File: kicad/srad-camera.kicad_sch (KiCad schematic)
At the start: 21 parts, among them J1 DEBUG, SW1 POWER, SW2 USER, SW3 BOOT0

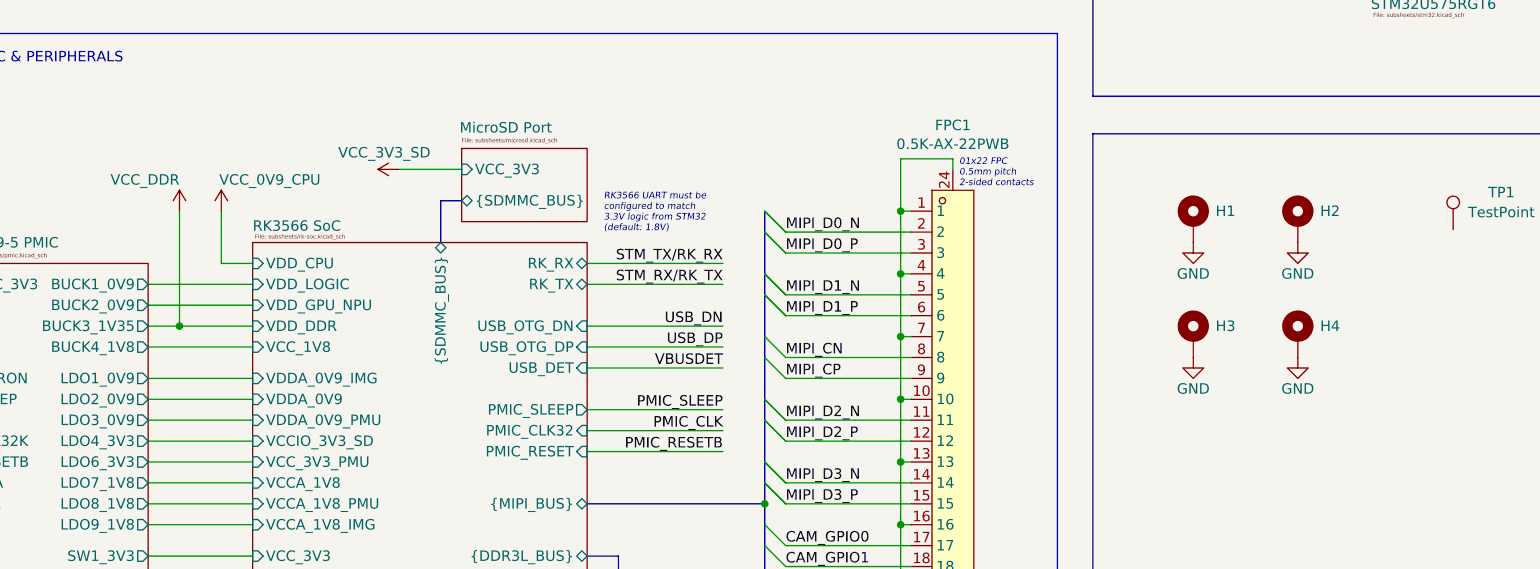
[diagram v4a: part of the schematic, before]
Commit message: All major components placed on board
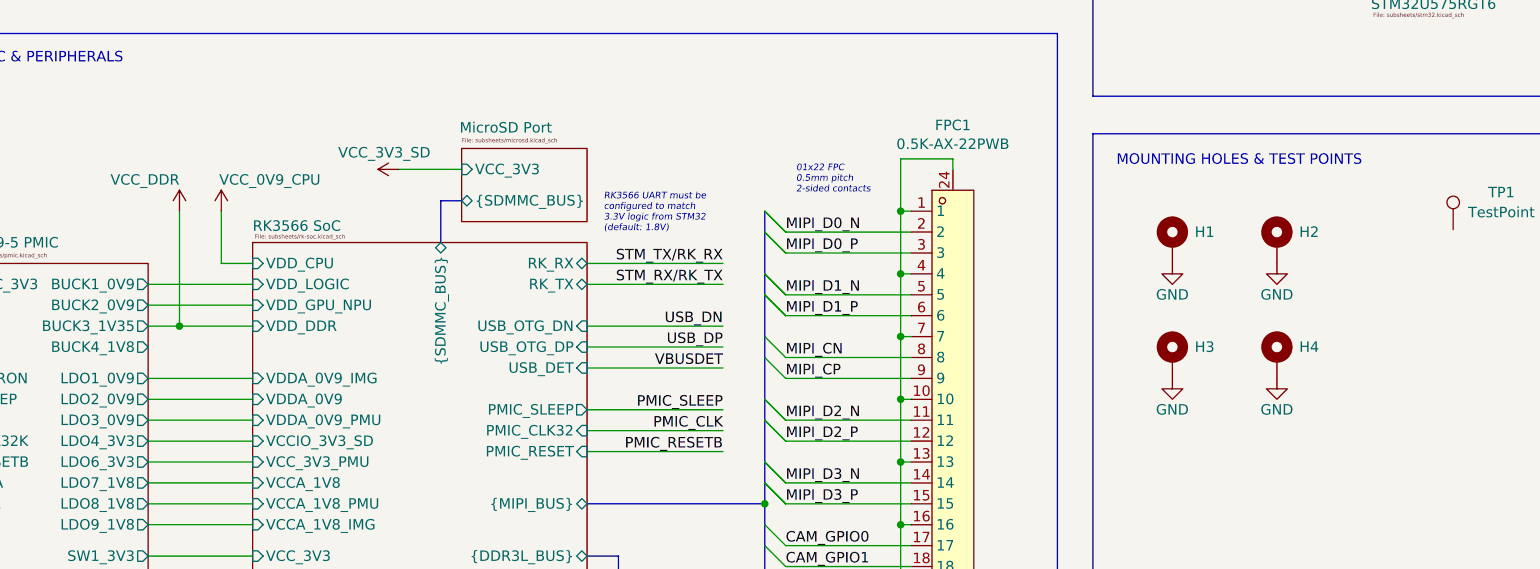
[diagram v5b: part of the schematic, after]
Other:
- sheet RK3566 SoC ports: added none; removed VCC_1V8
- note added: "MOUNTING HOLES & TEST POINTS"
- moved on the sheet: H1, H2, H3, H4
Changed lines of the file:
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@@
 	(text "01x22 FPC\n0.5mm pitch\n2-sided contacts"
 		(exclude_from_sim no)
-		(at 160.782 107.188 0)
+		(at 140.97 107.95 0)
 		(effects
 			(font
@@
 		)
 	)
+	(text "MOUNTING HOLES & TEST POINTS"
+		(exclude_from_sim no)
+		(at 194.818 105.664 0)
+		(effects
+			(font
+				(size 1.27 1.27)
+			)
+		)
+	)
 	(junction
 		(at 153.67 127)
@@
 		)
 	)
-	(wire
-		(pts
-			(xy 62.23 128.27) (xy 74.93 128.27)
-		)
-		(stroke
-			(width 0)
-			(type default)
-		)
-	)
 	(bus
 		(pts
@@
 		)
 	)
-	(rule_area
-		(polyline
-			(pts
-				(xy 150.4806 113.0631) (xy 153.0206 113.0631) (xy 153.0206 148.6231) (xy 150.4806 148.6231)
-			)
-			(stroke
-				(width 0)
-				(type dash)
-			)
-			(fill
-				(type none)
-			)
-		)
-	)
-	(netclass_flag ""
-		(length 2.54)
-		(shape round)
-		(at 151.7506 113.0631 0)
-		(fields_autoplaced yes)
-		(effects
-			(font
-				(size 1.27 1.27)
-			)
-			(justify left bottom)
-		)
-		(property "Netclass" "MIPI_DIFF"
-			(at 151.0521 110.5231 0)
-			(effects
-				(font
-					(size 1 1)
-					(italic yes)
-					(color 0 132 132 1)
-				)
-				(justify right)
-			)
-		)
-		(property "Component Class" ""
-			(at 320.6606 -2.5069 0)
-			(effects
-				(font
-					(size 1.27 1.27)
-					(italic yes)
-				)
-				(justify left)
-			)
-		)
-	)
 	(symbol
 		(lib_id "power:GND")
-		(at 189.23 115.57 0)
+		(at 186.69 118.11 0)
 		(unit 1)
 		(exclude_from_sim no)
@@
 		(dnp no)
 		(property "Reference" "#PWR013"
-			(at 189.23 121.92 0)
+			(at 186.69 124.46 0)
 			(effects
 				(font
@@
 		)
 		(property "Value" "GND"
-			(at 189.23 119.38 0)
+			(at 186.69 121.92 0)
 			(effects
 				(font
@@
 		)
 		(property "Footprint" ""
-			(at 189.23 115.57 0)
+			(at 186.69 118.11 0)
 			(effects
 				(font
@@
 		)
 		(property "Datasheet" ""
-			(at 189.23 115.57 0)
+			(at 186.69 118.11 0)
 			(effects
 				(font
@@
 		)
 		(property "Description" "Power symbol creates a global label with name \"GND\" , ground"
-			(at 189.23 115.57 0)
+			(at 186.69 118.11 0)
 			(effects
 				(font
@@
 		(lib_name "MountingHole_Pad_MP_1")
 		(lib_id "Mechanical:MountingHole_Pad_MP")
-		(at 189.23 113.03 0)
+		(at 186.69 115.57 0)
 		(unit 1)
 		(exclude_from_sim no)
@@
 		(fields_autoplaced yes)
 		(property "Reference" "H1"
-			(at 193.1512 111.76 0)
+			(at 190.6112 114.3 0)
 			(effects
 				(font
@@
 		)
 		(property "Value" "MntHole"
-			(at 202.3736 112.9721 0)
+			(at 199.8336 115.5121 0)
 			(effects
 				(font
@@
 		)
 		(property "Footprint" "srad-camera-footprints:4-40_MountingHole"
-			(at 189.23 113.03 0)
+			(at 186.69 115.57 0)
 			(effects
 				(font
@@
 		)
 		(property "Datasheet" "~"
-			(at 189.23 113.03 0)
+			(at 186.69 115.57 0)
 			(effects
 				(font
@@
 		)
 		(property "Description" "Mounting Hole with connection as pad named MP"
-			(at 189.23 113.03 0)
+			(at 186.69 115.57 0)
 			(effects
 				(font
@@
 	(symbol
 		(lib_id "power:GND")
-		(at 201.93 129.54 0)
+		(at 199.39 132.08 0)
 		(unit 1)
 		(exclude_from_sim no)
@@
 		(dnp no)
 		(property "Reference" "#PWR016"
-			(at 201.93 135.89 0)
+			(at 199.39 138.43 0)
 			(effects
 				(font
@@
 		)
 		(property "Value" "GND"
-			(at 201.93 133.35 0)
+			(at 199.39 135.89 0)
 			(effects
 				(font
@@
 		)
 		(property "Footprint" ""
-			(at 201.93 129.54 0)
+			(at 199.39 132.08 0)
 			(effects
 				(font
@@
 		)
 		(property "Datasheet" ""
-			(at 201.93 129.54 0)
+			(at 199.39 132.08 0)
 			(effects
 				(font
@@
 		)
 		(property "Description" "Power symbol creates a global label with name \"GND\" , ground"
-			(at 201.93 129.54 0)
+			(at 199.39 132.08 0)
 			(effects
 				(font
@@
 		(lib_name "MountingHole_Pad_MP_1")
 		(lib_id "Mechanical:MountingHole_Pad_MP")
-		(at 201.93 113.03 0)
+		(at 199.39 115.57 0)
 		(unit 1)
 		(exclude_from_sim no)
@@
 		(fields_autoplaced yes)
 		(property "Reference" "H2"
-			(at 205.8512 111.76 0)
+			(at 203.3112 114.3 0)
 			(effects
 				(font
@@
 		)
 		(property "Value" "MntHole"
-			(at 215.0736 112.9721 0)
+			(at 212.5336 115.5121 0)
 			(effects
 				(font
@@
 		)
 		(property "Footprint" "srad-camera-footprints:4-40_MountingHole"
-			(at 201.93 113.03 0)
+			(at 199.39 115.57 0)
 			(effects
 				(font
@@
 		)
 		(property "Datasheet" "~"
-			(at 201.93 113.03 0)
+			(at 199.39 115.57 0)
 			(effects
 				(font
@@
 		)
 		(property "Description" "Mounting Hole with connection as pad named MP"
-			(at 201.93 113.03 0)
+			(at 199.39 115.57 0)
 			(effects
 				(font
@@
 	(symbol
 		(lib_id "power:GND")
-		(at 189.23 129.54 0)
+		(at 186.69 132.08 0)
 		(unit 1)
 		(exclude_from_sim no)
@@
 		(dnp no)
 		(property "Reference" "#PWR015"
-			(at 189.23 135.89 0)
+			(at 186.69 138.43 0)
 			(effects
 				(font
@@
 		)
 		(property "Value" "GND"
-			(at 189.23 133.35 0)
+			(at 186.69 135.89 0)
 			(effects
 				(font
@@
 		)
 		(property "Footprint" ""
-			(at 189.23 129.54 0)
+			(at 186.69 132.08 0)
 			(effects
 				(font
@@
 		)
 		(property "Datasheet" ""
-			(at 189.23 129.54 0)
+			(at 186.69 132.08 0)
 			(effects
 				(font
@@
 		)
 		(property "Description" "Power symbol creates a global label with name \"GND\" , ground"
-			(at 189.23 129.54 0)
+			(at 186.69 132.08 0)
 			(effects
 				(font
@@
 		(lib_name "MountingHole_Pad_MP_1")
 		(lib_id "Mechanical:MountingHole_Pad_MP")
-		(at 201.93 127 0)
+		(at 199.39 129.54 0)
 		(unit 1)
 		(exclude_from_sim no)
@@
 		(fields_autoplaced yes)
 		(property "Reference" "H4"
-			(at 205.8512 125.73 0)
+			(at 203.3112 128.27 0)
 			(effects
 				(font
@@
 		)
 		(property "Value" "MntHole"
-			(at 215.0736 126.9421 0)
+			(at 212.5336 129.4821 0)
 			(effects
 				(font
@@
 		)
 		(property "Footprint" "srad-camera-footprints:4-40_MountingHole"
-			(at 201.93 127 0)
+			(at 199.39 129.54 0)
 			(effects
 				(font
@@
 		)
 		(property "Datasheet" "~"
-			(at 201.93 127 0)
+			(at 199.39 129.54 0)
 			(effects
 				(font
@@
 		)
 		(property "Description" "Mounting Hole with connection as pad named MP"
-			(at 201.93 127 0)
+			(at 199.39 129.54 0)
 			(effects
 				(font
@@
 		(lib_name "MountingHole_Pad_MP_1")
 		(lib_id "Mechanical:MountingHole_Pad_MP")
-		(at 189.23 127 0)
+		(at 186.69 129.54 0)
 		(unit 1)
 		(exclude_from_sim no)
@@
 		(fields_autoplaced yes)
 		(property "Reference" "H3"
-			(at 193.1512 125.73 0)
+			(at 190.6112 128.27 0)
 			(effects
 				(font
@@
 		)
 		(property "Value" "MntHole"
-			(at 202.3736 126.9421 0)
+			(at 199.8336 129.4821 0)
 			(effects
 				(font
@@
 		)
 		(property "Footprint" "srad-camera-footprints:4-40_MountingHole"
-			(at 189.23 127 0)
+			(at 186.69 129.54 0)
 			(effects
 				(font
@@
 		)
 		(property "Datasheet" "~"
-			(at 189.23 127 0)
+			(at 186.69 129.54 0)
 			(effects
 				(font
@@
 		)
 		(property "Description" "Mounting Hole with connection as pad named MP"
-			(at 189.23 127 0)
+			(at 186.69 129.54 0)
 			(effects
 				(font
@@
 	(symbol
 		(lib_id "power:GND")
-		(at 201.93 115.57 0)
+		(at 199.39 118.11 0)
 		(unit 1)
 		(exclude_from_sim no)
@@
 		(dnp no)
 		(property "Reference" "#PWR014"
-			(at 201.93 121.92 0)
+			(at 199.39 124.46 0)
 			(effects
 				(font
@@
 		)
 		(property "Value" "GND"
-			(at 201.93 119.38 0)
+			(at 199.39 121.92 0)
 			(effects
 				(font
@@
 		)
 		(property "Footprint" ""
-			(at 201.93 115.57 0)
+			(at 199.39 118.11 0)
 			(effects
 				(font
@@
 		)
 		(property "Datasheet" ""
-			(at 201.93 115.57 0)
+			(at 199.39 118.11 0)
 			(effects
 				(font
@@
 		)
 		(property "Description" "Power symbol creates a global label with name \"GND\" , ground"
-			(at 201.93 115.57 0)
+			(at 199.39 118.11 0)
 			(effects
 				(font
@@
 			(effects
 				(font
-					(size 1.27 1.27)
-				)
-				(justify left)
-			)
-		)
-		(pin "VCC_1V8" input
-			(at 74.93 128.27 180)
-			(effects
-				(font

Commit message: Allllmost everything placed
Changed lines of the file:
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@@
 	)
 	(junction
+		(at 259.08 78.74)
+		(diameter 0)
+		(color 0 0 0 0)
+	)
+	(junction
 		(at 147.32 170.18)
 		(diameter 0)
@@
 	(wire
 		(pts
+			(xy 259.08 78.74) (xy 259.08 80.01)
+		)
+		(stroke
+			(width 0)
+			(type default)
+		)
+	)
+	(wire
+		(pts
 			(xy 160.02 170.18) (xy 160.02 171.45)
 		)
@@
 	(wire
 		(pts
+			(xy 259.08 77.47) (xy 259.08 78.74)
+		)
+		(stroke
+			(width 0)
+			(type default)
+		)
+	)
+	(wire
+		(pts
 			(xy 199.39 57.15) (xy 210.82 57.15)
 		)
@@
 	(wire
 		(pts
+			(xy 260.35 78.74) (xy 259.08 78.74)
+		)
+		(stroke
+			(width 0)
+			(type default)
+		)
+	)
+	(wire
+		(pts
 			(xy 115.57 156.21) (xy 118.11 156.21)
 		)
@@
 		(lib_name "VCC_9")
 		(lib_id "power:VCC")
-		(at 259.08 77.47 270)
+		(at 260.35 78.74 270)
 		(unit 1)
 		(exclude_from_sim no)
@@
 		(dnp no)
 		(property "Reference" "#PWR07"
-			(at 255.27 77.47 0)
+			(at 256.54 78.74 0)
 			(effects
 				(font
@@
 		)
 		(property "Value" "VCCIO_3V3_IMU"
-			(at 262.128 77.47 90)
+			(at 263.398 78.74 90)
 			(effects
 				(font
@@
 		)
 		(property "Footprint" ""
-			(at 259.08 77.47 0)
+			(at 260.35 78.74 0)
 			(effects
 				(font
@@
 		)
 		(property "Datasheet" ""
-			(at 259.08 77.47 0)
+			(at 260.35 78.74 0)
 			(effects
 				(font
@@
 		)
 		(property "Description" "Power symbol creates a global label with name \"VCC\""
-			(at 259.08 77.47 0)
+			(at 260.35 78.74 0)
 			(effects
 				(font
@@
 					(unit 1)
 				)
-			)
-		)
-	)
-	(symbol
-		(lib_id "power:VCC")
-		(at 259.08 80.01 270)
-		(unit 1)
-		(exclude_from_sim no)
-		(in_bom yes)
-		(on_board yes)
-		(dnp no)
-		(property "Reference" "#PWR08"
-			(at 255.27 80.01 0)
-			(effects
-				(font
-					(size 1.27 1.27)
-				)
-				(hide yes)
-			)
-		)
-		(property "Value" "VCC_3V3_SYS"
-			(at 262.128 80.01 90)
-			(effects
-				(font
-					(size 1.27 1.27)
-				)
-				(justify left)
-			)
-		)
-		(property "Footprint" ""
-			(at 259.08 80.01 0)
-			(effects
-				(font
-					(size 1.27 1.27)
-				)
-				(hide yes)
-			)
-		)
-		(property "Datasheet" ""
-			(at 259.08 80.01 0)
-			(effects
-				(font
-					(size 1.27 1.27)
-				)
-				(hide yes)
-			)
-		)
-		(property "Description" "Power symbol creates a global label with name \"VCC\""
-			(at 259.08 80.01 0)
-			(effects
-				(font
-					(size 1.27 1.27)
-				)
-				(hide yes)
-			)
-		)
-		(pin "1"
-		)
-		(instances
-			(project "srad-camera"
-				(path "/da62c771-e8c9-451f-8df1-ec995aadcb11"
-					(reference "#PWR08")
-					(unit 1)
-				)

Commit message: PCB done besides fixing screwups + length matching
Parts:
- FPC1: value 0.5K-AX-22PWB -> Amphenol_F32R 1x22; footprint srad-camera-footprints:FPC-SMD_22P-P0.50_HDGC_0.5K-AX-22PWB -> srad-camera-footprints:AMPHENOL_10051922-2210ELF
- SW1: value POWER -> PWR
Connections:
- net VCC_3V3_SYS: now also SW1.3 (C); no longer SW1.1 (A)
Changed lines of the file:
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@@
 	)
 	(no_connect
-		(at 74.93 43.18)
+		(at 199.39 36.83)
 	)
 	(no_connect
-		(at 201.93 36.83)
+		(at 74.93 43.18)
 	)
 	(bus_entry
@@
 	(wire
 		(pts
-			(xy 199.39 35.56) (xy 199.39 36.83)
-		)
-		(stroke
-			(width 0)
-			(type default)
-		)
-	)
-	(wire
-		(pts
 			(xy 115.57 140.97) (xy 132.08 140.97)
 		)
@@
 	(wire
 		(pts
+			(xy 201.93 35.56) (xy 201.93 36.83)
+		)
+		(stroke
+			(width 0)
+			(type default)
+		)
+	)
+	(wire
+		(pts
 			(xy 115.57 118.11) (xy 132.08 118.11)
 		)
@@
 			)
 		)
-		(property "Value" "POWER"
+		(property "Value" "PWR"
 			(at 197.612 40.64 90)
 			(effects
@@
 		(lib_name "VCC_11")
 		(lib_id "power:VCC")
-		(at 199.39 35.56 0)
+		(at 201.93 35.56 0)
 		(unit 1)
 		(exclude_from_sim no)
@@
 		(dnp no)
 		(property "Reference" "#PWR01"
-			(at 199.39 39.37 0)
+			(at 201.93 39.37 0)
 			(effects
 				(font
@@
 		)
 		(property "Value" "VCC_3V3_SYS"
-			(at 199.39 31.496 0)
+			(at 201.93 31.496 0)
 			(effects
 				(font
@@
 		)
 		(property "Footprint" ""
-			(at 199.39 35.56 0)
+			(at 201.93 35.56 0)
 			(effects
 				(font
@@
 		)
 		(property "Datasheet" ""
-			(at 199.39 35.56 0)
+			(at 201.93 35.56 0)
 			(effects
 				(font
@@
 		)
 		(property "Description" "Power symbol creates a global label with name \"VCC\""
-			(at 199.39 35.56 0)
+			(at 201.93 35.56 0)
 			(effects
 				(font
@@
 			)
 		)
-		(property "Value" "0.5K-AX-22PWB"
+		(property "Value" "Amphenol_F32R 1x22"
 			(at 160.02 102.87 0)
 			(effects
@@
 			)
 		)
-		(property "Footprint" "srad-camera-footprints:FPC-SMD_22P-P0.50_HDGC_0.5K-AX-22PWB"
+		(property "Footprint" "srad-camera-footprints:AMPHENOL_10051922-2210ELF"
 			(at 160.02 138.43 0)
 			(effects

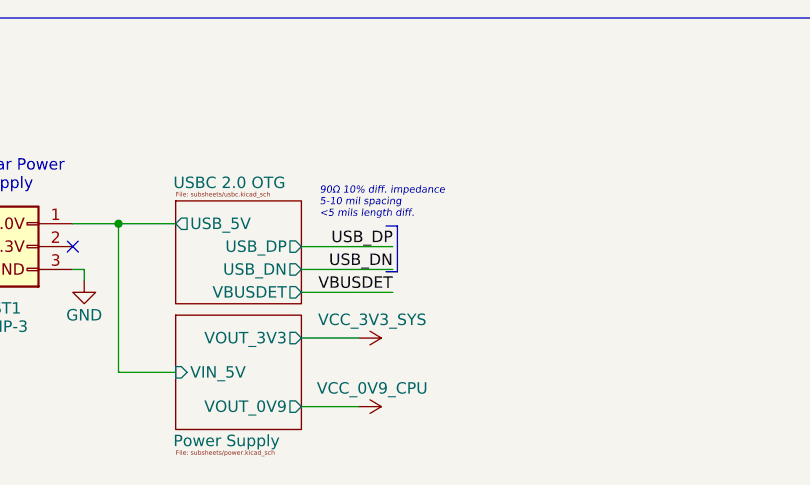
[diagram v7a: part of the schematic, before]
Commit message: Length matching for DDL3 UDQS
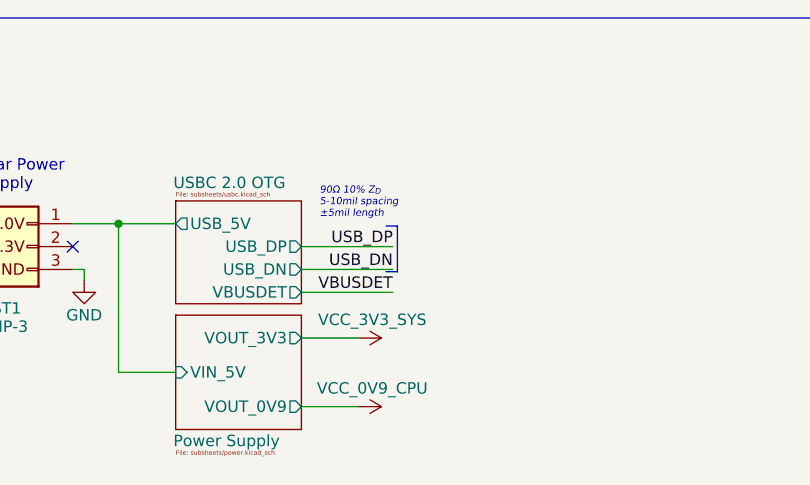
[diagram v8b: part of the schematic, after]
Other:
- note added: "90Ω 10% Z_{D} 5-10mil spacing ±5mil length"
- note removed: "90Ω 10% diff. impedance 5-10 mil spacing <5 mils length diff."
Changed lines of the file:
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@@
 		)
 	)
-	(text "90Ω 10% diff. impedance\n5-10 mil spacing\n<5 mils length diff."
+	(text "90Ω 10% Z_{D}\n5-10mil spacing\n±5mil length"
 		(exclude_from_sim no)
 		(at 102.362 38.354 0)
